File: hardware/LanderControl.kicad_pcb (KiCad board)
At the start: 4 copper layers, 140 x 54 mm, 161 parts, among them J2 Conn_01x04, J3 Conn_01x05, J5 MEM2051-00-195-00-A, Q1 BC846, Q2 BC846, Q3 BC846, Q4 BC846, Q5 BC846, Q6 BC846, Q7 BC846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

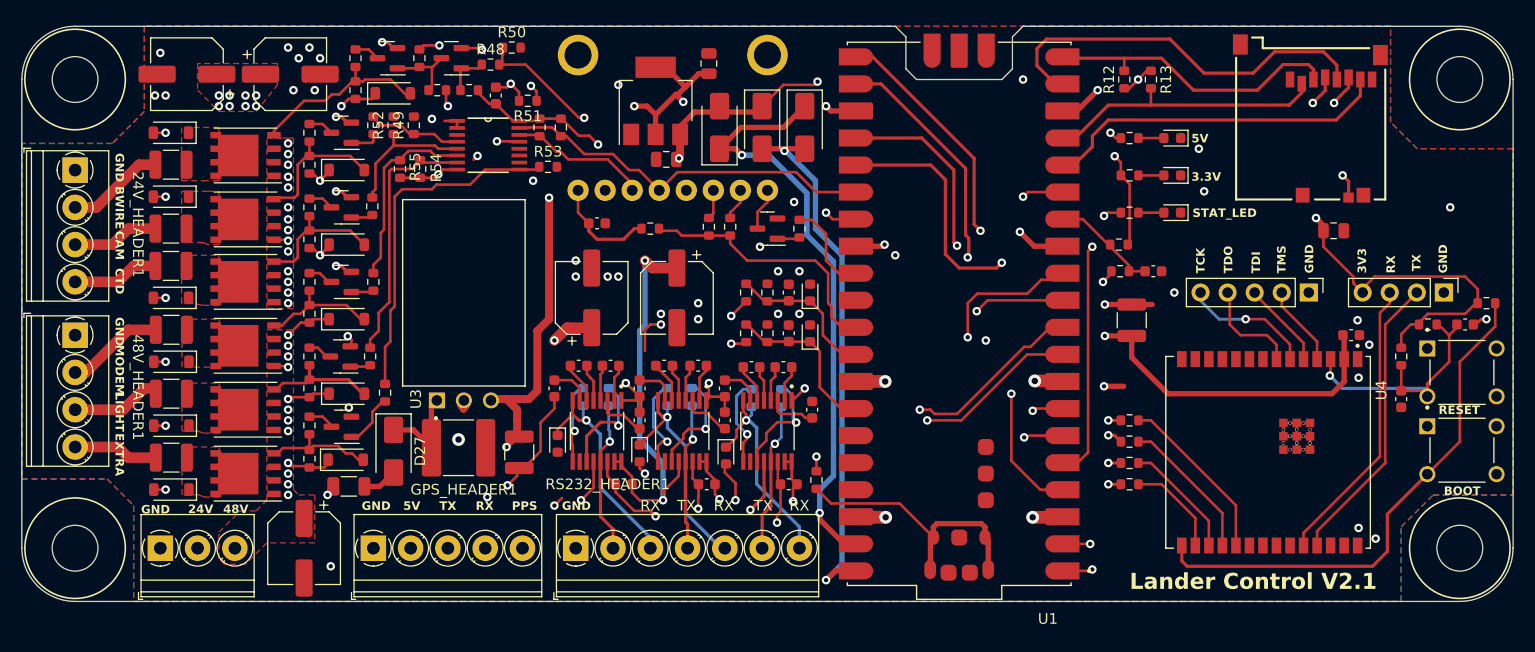
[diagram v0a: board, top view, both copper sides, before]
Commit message: Clean up silkscreen labels
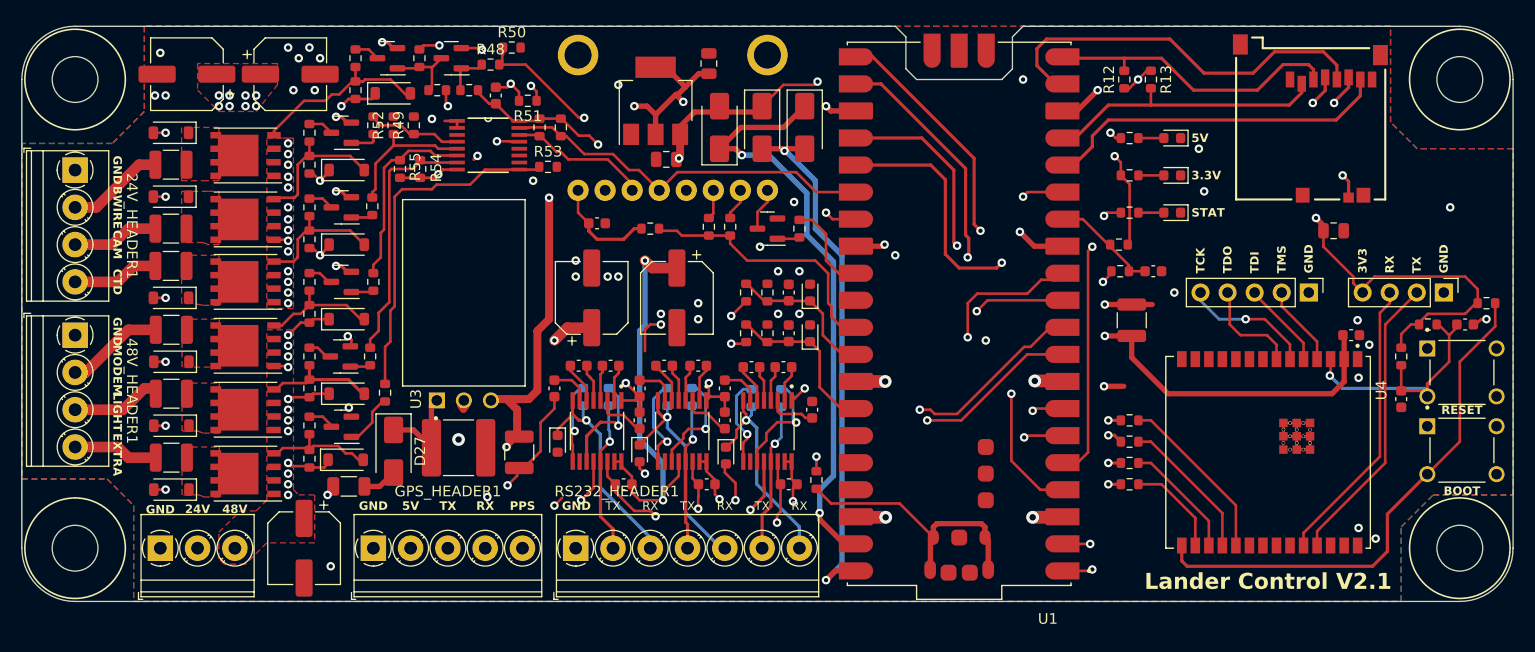
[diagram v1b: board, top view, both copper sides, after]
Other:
- board text added: "STAT"
- board text removed: "STAT_LED"
